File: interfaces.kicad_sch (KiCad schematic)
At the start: 86 parts, among them IC3 TPD8S009DSMR, J4 WE_629105150521, J6 685119134923, J7 1140084168, Q2 BSS138APW, Q3 BSS138APW, Q4 BSS138APW, Q5 BSS138APW, Q6 BSS138APW, U7 FT4232HQ, U8 SRST, Y2 ABM8G-12.000MHZ-18-D2Y-T

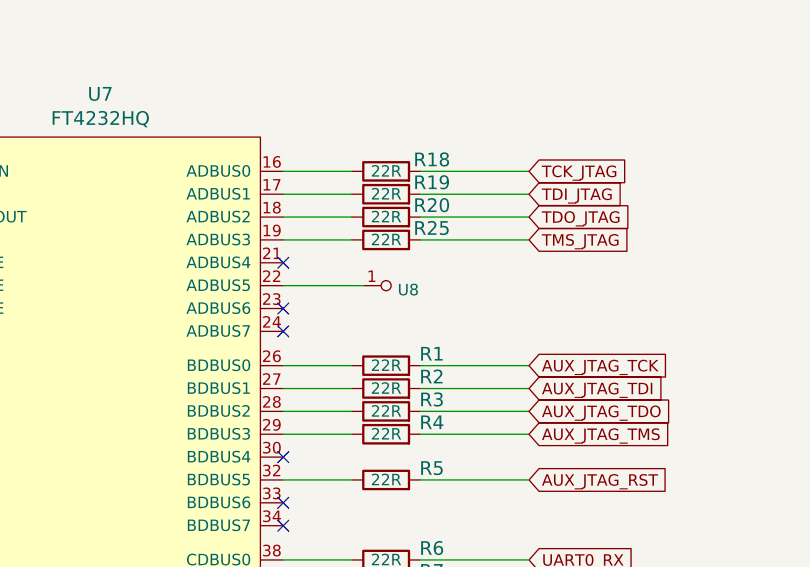
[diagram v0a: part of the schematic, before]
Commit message: Fix broken test-points
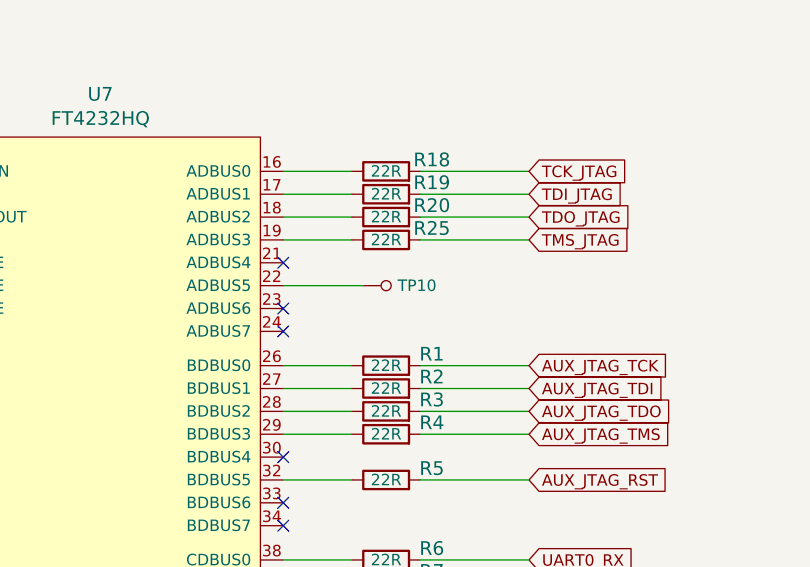
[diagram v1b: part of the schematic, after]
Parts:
- removed U8: SRST, symbol lpddr4-test-board:test
- added TP10: TP_SMD1MM, lpddr4-test-board-footprints:Testpoint_smd_1mm, symbol lpddr4-test-board:TP_SMD1MM
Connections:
- net at U7.22 (ADBUS5): now also TP10.1
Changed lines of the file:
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@@
     (pin "2")
-  )
-  (symbol (lib_id "lpddr4-test-board:test") (at 144.78 87.63 90) (unit 1)
-    (in_bom yes) (on_board yes)
-    (property "Reference" "U8" (id 0) (at 143.51 89.3826 90)
-      (effects (font (size 1.27 1.27)) (justify right))
-    )
-    (property "Value" "SRST" (id 1) (at 143.51 90.5256 90)
-      (effects (font (size 1.27 1.27)) (justify right) hide)
-    )
-    (property "Footprint" "" (id 2) (at 144.78 87.63 0)
-      (effects (font (size 1.27 1.27)) hide)
-    )
-    (property "Datasheet" "" (id 3) (at 144.78 87.63 0)
-      (effects (font (size 1.27 1.27)) hide)
-    )
-    (pin "1")
   )
   (symbol (lib_id "lpddr4-test-board:GND") (at 339.725 107.315 0) (unit 1)
@@
     )
     (pin "1")
+  )
+  (symbol (lib_id "lpddr4-test-board:TP_SMD1MM") (at 142.24 88.9 90) (unit 1)
+    (in_bom yes) (on_board yes)
+    (property "Reference" "TP10" (id 0) (at 143.51 88.9 90)
+      (effects (font (size 1.27 1.27)) (justify right))
+    )
+    (property "Value" "TP_SMD1MM" (id 1) (at 144.78 88.9 0)
+      (effects (font (size 1.27 1.27)) hide)
+    )
+    (property "Footprint" "lpddr4-test-board-footprints:Testpoint_smd_1mm" (id 2) (at 137.16 83.82 0)
+      (effects (font (size 1.524 1.524)) (justify left) hide)
+    )
+    (property "Datasheet" "" (id 3) (at 134.62 83.82 0)
+      (effects (font (size 1.524 1.524)) (justify left) hide)
+    )
+    (pin "1")

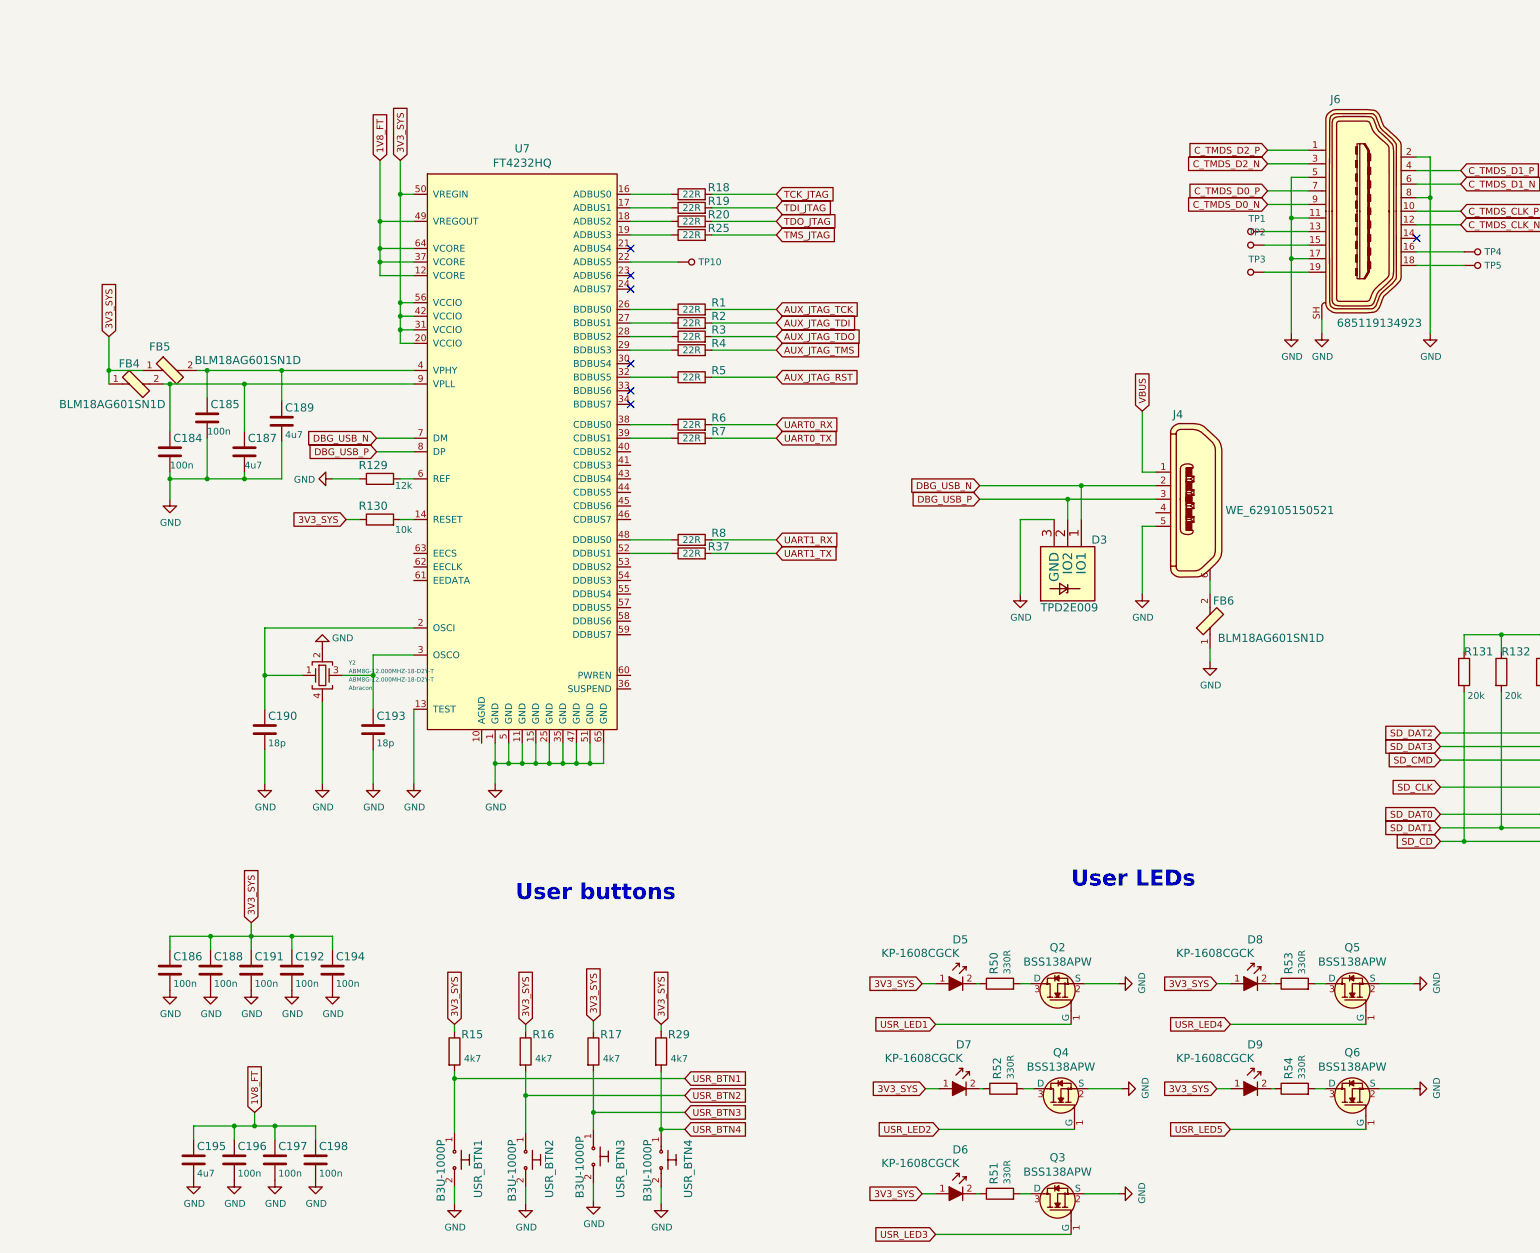
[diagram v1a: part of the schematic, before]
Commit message: Replace FT2232H-56Q with FT4232H-56Q
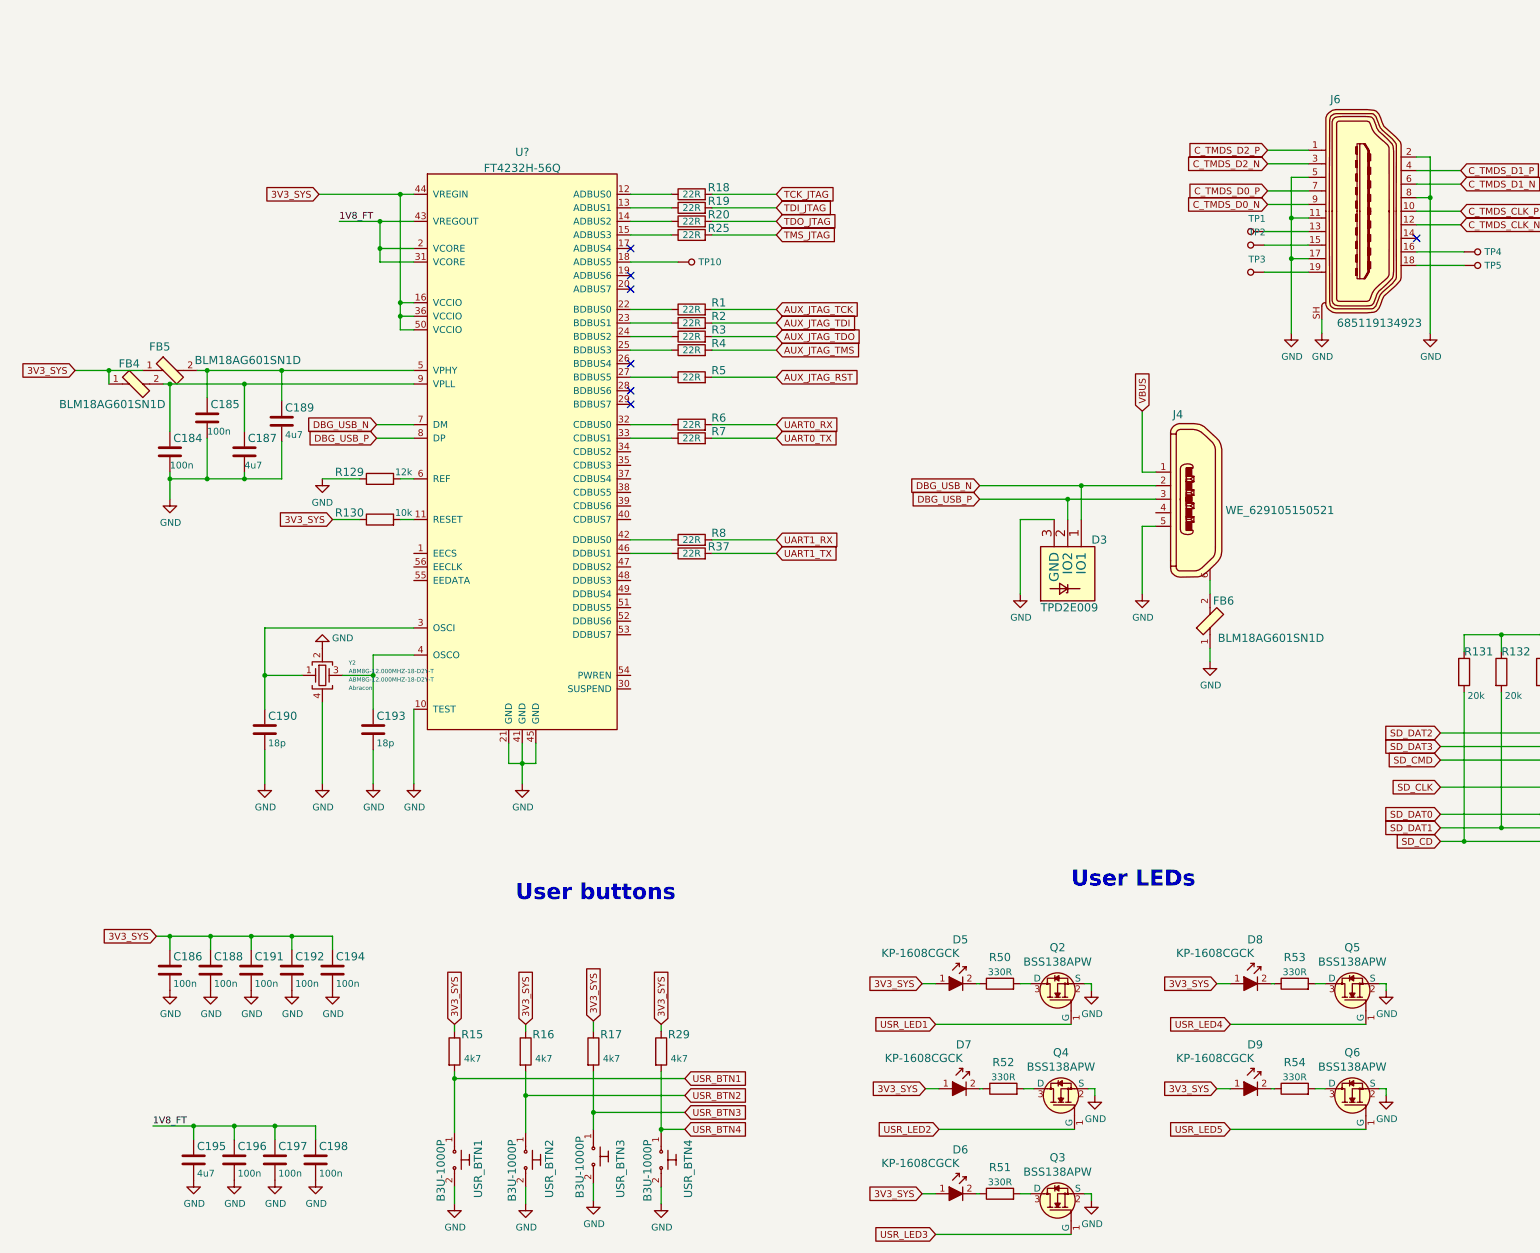
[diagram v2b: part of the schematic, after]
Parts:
- removed U7: FT4232HQ, lpddr4-test-board-footprints:FT4232HQ, symbol lpddr4-test-board:FT4232HQ
- added U?: FT4232H-56Q, antmicro-footprints:QFN-56-1EP_8x8mm_P0.5mm_EP5.5.9x5.9mm, symbol antmicroInterfaceControllers:FT4232H-56Q
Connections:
- net 1V8_FT: now also U?.2 (VCORE), U?.31 (VCORE), U?.43 (VREGOUT)
- net 3V3_SYS: now also U?.16 (VCCIO), U?.36 (VCCIO), U?.44 (VREGIN), U?.50 (VCCIO)
- net DBG_USB_N: now also U?.7 (DM)
- net DBG_USB_P: now also U?.8 (DP)
- net GND: now also U?.10 (TEST), U?.21 (GND), U?.41 (GND), U?.45 (GND)
- net at R1.1: now also U?.22 (BDBUS0)
- net at R2.1: now also U?.23 (BDBUS1)
- net at R3.1: now also U?.24 (BDBUS2)
- net at R4.1: now also U?.25 (BDBUS3)
- net at R6.1: now also U?.32 (CDBUS0)
- net at R37.1: now also U?.46 (DDBUS1)
- net at R7.1: now also U?.33 (CDBUS1)
- net at R8.1: now also U?.42 (DDBUS0)
- net at C185.1, C189.1, FB5.2: now also U?.5 (VPHY)
- net at C184.1, C187.1, FB4.2: now also U?.9 (VPLL)
- net at R129.2: now also U?.6 (REF)
- net at R130.2: now also U?.11 (RESET)
- net at C190.1, Y2.1: now also U?.3 (OSCI)
- net at C193.1, Y2.3: now also U?.4 (OSCO)
- net at R18.1: now also U?.12 (ADBUS0)
- net at R19.1: now also U?.13 (ADBUS1)
- net at R20.1: now also U?.14 (ADBUS2)
- net at R25.1: now also U?.15 (ADBUS3)
- net at TP10.1: now also U?.18 (ADBUS5)
- net at R5.1: now also U?.27 (BDBUS5)

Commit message: Placement and routing of FT4232H. Re annotation of the schematics
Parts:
- removed C191, C198: C_100n_0402_6V3, lpddr4-test-board-footprints:0402-cap, symbol lpddr4-test-board:C_100n_0402_6V3
- gave numbers to parts that had none: 1
- renumbered C195 to C10, C185 to C11, C188 to C12, C196 to C13, C187 to C14, C190 to C16, C197 to C17, C189 to C18, C192 to C19, C194 to C21, C193 to C22, C10 to C23, C184 to C8, C186 to C9, D5 to D1, D6 to D2, D7 to D3, D3 to D4, D8 to D5, D9 to D6, FB4 to FB1, FB5 to FB2, FB6 to FB3, IC3 to IC1, J4 to J1, J6 to J2, J7 to J3, Q2 to Q1, Q3 to Q2, Q4 to Q3, Q5 to Q4, Q6 to Q5, R16 to R10, R17 to R11, R29 to R12, R18 to R13, R19 to R14, R20 to R15, R25 to R16, R1 to R17, R2 to R18, R3 to R19, R4 to R20, R5 to R21, R6 to R22, R7 to R23, R8 to R24, R37 to R25, R50 to R26, R51 to R27, R52 to R28, R53 to R29, R54 to R30, R131 to R31, R132 to R32, R133 to R33, R134 to R34, R135 to R35, R136 to R36, R137 to R37, R138 to R38, R139 to R39, R140 to R40, R141 to R41, R142 to R42, R143 to R43, R144 to R44, R145 to R45, R146 to R46, R129 to R7, R130 to R8, R15 to R9, TP10 to TP1, TP1 to TP2, TP2 to TP3, TP3 to TP4, TP4 to TP5, TP5 to TP6, Y2 to Y1
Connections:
- no-connect marks 7 -> 22
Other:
- moved on the sheet: C19, C21
